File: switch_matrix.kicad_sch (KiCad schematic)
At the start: 8 parts, among them SW1 MX_SW_solder, SW2 MX_SW_solder, SW3 MX_SW_solder, SW4 MX_SW_solder

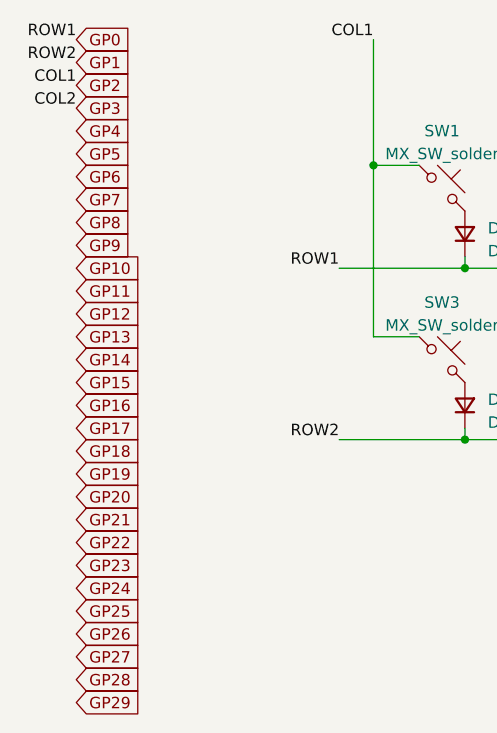
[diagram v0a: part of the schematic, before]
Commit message: update to kicad 8
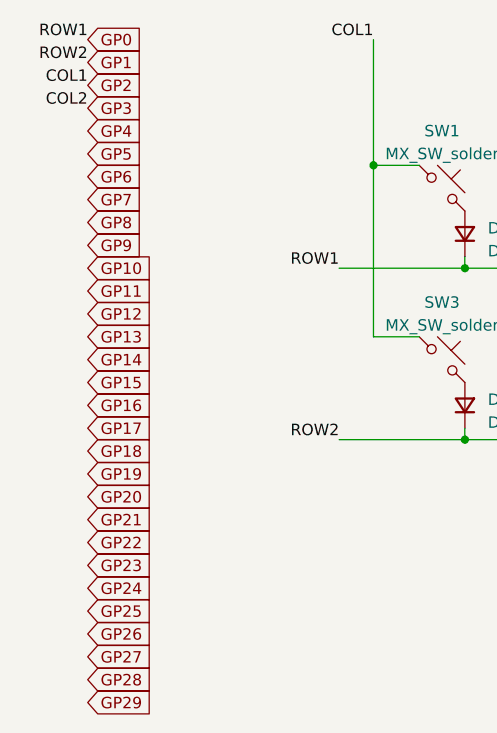
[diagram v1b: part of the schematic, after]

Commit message: keyboard switch comletion
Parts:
- removed D2, D4: D_Small, Diode_SMD:D_SOD-123, symbol Device:D_Small
- removed SW2, SW4: MX_SW_solder, marbastlib-mx:SW_MX_1u, symbol marbastlib-mx:MX_SW_solder
- added D203, D204, D205, D206, D207, D208, D209, D210, D211, D212, D213, D214, D215, D216, D217, D218, D219, D220, D221, D222, D223, D224, D225, D226, D227, D228, D229, D230, D231, D232, D233, D234, D235, D236, D237, D238, D239, D240, D241, D242, D243, D244, D245, D246, D247, D248, D249, D250, D251, D252, D253, D254, D255, D256, D257, D258, D259, D260, D261: D_Small, Diode_SMD:D_SOD-123, symbol Device:D_Small
- added SW203, SW204, SW205, SW206, SW207, SW208, SW209, SW210, SW211, SW212, SW213, SW214, SW215, SW216, SW217, SW218, SW219, SW220, SW221, SW222, SW223, SW224, SW225, SW226, SW227, SW228, SW229, SW230, SW231, SW232, SW233, SW234, SW235, SW236, SW237, SW238, SW239, SW240, SW241, SW242, SW243, SW244, SW245, SW246, SW247, SW248, SW249, SW250, SW251, SW252, SW253, SW254, SW255, SW256, SW257, SW258, SW259, SW260, SW261: MX_SW_solder, marbastlib-mx:SW_MX_1u, symbol marbastlib-mx:MX_SW_solder
- renumbered D1 to D201, D3 to D202, SW1 to SW201, SW3 to SW202
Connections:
- net GP0: now also SW201.1, SW202.1, SW203.1, SW204.1, SW205.1; no longer D201.1 (K)
- net GP1: now also SW206.1, SW207.1, SW208.1, SW209.1, SW210.1; no longer D202.1 (K)
- net GP10: now also SW246.1, SW247.1, SW248.1, SW249.1, SW250.1
- net GP11: now also SW251.1, SW252.1, SW253.1
- net GP12: now also SW255.1, SW256.1
- net GP13: now also SW257.1, SW258.1, SW259.1, SW260.1, SW261.1
- net GP14: now also D201.1 (K), D206.1 (K), D211.1 (K), D216.1 (K), D220.1 (K), D224.1 (K), D229.1 (K), D233.1 (K), D237.1 (K), D241.1 (K), D246.1 (K), D251.1 (K), D255.1 (K), D257.1 (K)
- net GP15: now also D202.1 (K), D207.1 (K), D212.1 (K), D217.1 (K), D221.1 (K), D225.1 (K), D230.1 (K), D234.1 (K), D238.1 (K), D242.1 (K), D247.1 (K), D252.1 (K), D256.1 (K), D258.1 (K)
- net GP16: now also D203.1 (K), D208.1 (K), D213.1 (K), D218.1 (K), D222.1 (K), D226.1 (K), D231.1 (K), D235.1 (K), D239.1 (K), D243.1 (K), D248.1 (K), D253.1 (K), D259.1 (K)
- net GP17: now also D204.1 (K), D209.1 (K), D214.1 (K), D219.1 (K), D223.1 (K), D227.1 (K), D232.1 (K), D236.1 (K), D240.1 (K), D244.1 (K), D249.1 (K), D260.1 (K)
- net GP18: now also D205.1 (K), D210.1 (K), D215.1 (K), D228.1 (K), D245.1 (K), D250.1 (K), D254.1 (K), D261.1 (K)
- net GP2: now also SW211.1, SW212.1, SW213.1, SW214.1, SW215.1; no longer SW201.1, SW202.1
- net GP3: now also SW216.1, SW217.1, SW218.1, SW219.1
- net GP4: now also SW220.1, SW221.1, SW222.1, SW223.1
- net GP5: now also SW224.1, SW225.1, SW226.1, SW227.1, SW228.1
- net GP6: now also SW229.1, SW230.1, SW231.1, SW232.1
- net GP7: now also SW233.1, SW234.1, SW235.1, SW236.1
- net GP8: now also SW237.1, SW238.1, SW239.1, SW240.1
- net GP9: now also SW241.1, SW242.1, SW243.1, SW244.1, SW245.1
- new net: D209.2 (A), SW209.2
- new net: D226.2 (A), SW226.2
- new net: D211.2 (A), SW211.2
- new net: D224.2 (A), SW224.2
- new net: D239.2 (A), SW239.2
- new net: D210.2 (A), SW210.2
- new net: D260.2 (A), SW260.2
- new net: D238.2 (A), SW238.2
- new net: D230.2 (A), SW230.2
- new net: D229.2 (A), SW229.2
- new net: D242.2 (A), SW242.2
- new net: D250.2 (A), SW250.2
- new net: D255.2 (A), SW255.2
- new net: D228.2 (A), SW228.2
- new net: D261.2 (A), SW261.2
- new net: D240.2 (A), SW240.2
- new net: D246.2 (A), SW246.2
- new net: D212.2 (A), SW212.2
- new net: D247.2 (A), SW247.2
- new net: D218.2 (A), SW218.2
- new net: D258.2 (A), SW258.2
- new net: D249.2 (A), SW249.2
- new net: D248.2 (A), SW248.2
- new net: D220.2 (A), SW220.2
- new net: D206.2 (A), SW206.2
- new net: D243.2 (A), SW243.2
- new net: D251.2 (A), SW251.2
- new net: D259.2 (A), SW259.2
- new net: D204.2 (A), SW204.2
- new net: D217.2 (A), SW217.2
- new net: D233.2 (A), SW233.2
- new net: D235.2 (A), SW235.2
- new net: D215.2 (A), SW215.2
- new net: D253.2 (A), SW253.2
- new net: D236.2 (A), SW236.2
- new net: D245.2 (A), SW245.2
- new net: D254.2 (A), SW254.2
- new net: D237.2 (A), SW237.2
- new net: D241.2 (A), SW241.2
- new net: D222.2 (A), SW222.2
- new net: D221.2 (A), SW221.2
- new net: D252.2 (A), SW252.2
- new net: D244.2 (A), SW244.2
- new net: D232.2 (A), SW232.2
- new net: D205.2 (A), SW205.2
- new net: D207.2 (A), SW207.2
- new net: D219.2 (A), SW219.2
- new net: D213.2 (A), SW213.2
- new net: D223.2 (A), SW223.2
- new net: D216.2 (A), SW216.2
- new net: D227.2 (A), SW227.2
- new net: D256.2 (A), SW256.2
- new net: D214.2 (A), SW214.2
- new net: D257.2 (A), SW257.2
- new net: D208.2 (A), SW208.2
- new net: D225.2 (A), SW225.2
- new net: D231.2 (A), SW231.2
- new net: D203.2 (A), SW203.2
- new net: D234.2 (A), SW234.2

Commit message: push de modification
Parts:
- A1: renamed from SW208; value MX_SW_solder -> LP Gateron; footprint marbastlib-mx:SW_MX_1u -> key_switch:SW_Gateron_LowProfile_THT
- B1: renamed from SW227; value MX_SW_solder -> LP Gateron; footprint marbastlib-mx:SW_MX_1u -> key_switch:SW_Gateron_LowProfile_THT
- C18: renamed from SW219; value MX_SW_solder -> LP Gateron; footprint marbastlib-mx:SW_MX_1u -> key_switch:SW_Gateron_LowProfile_THT
- D18: renamed from SW218; value MX_SW_solder -> LP Gateron; footprint marbastlib-mx:SW_MX_1u -> key_switch:SW_Gateron_LowProfile_THT
- E1: renamed from SW217; value MX_SW_solder -> LP Gateron; footprint marbastlib-mx:SW_MX_1u -> key_switch:SW_Gateron_LowProfile_THT
- F1: renamed from SW222; value MX_SW_solder -> LP Gateron; footprint marbastlib-mx:SW_MX_1u -> key_switch:SW_Gateron_LowProfile_THT
- G1: renamed from SW226; value MX_SW_solder -> LP Gateron; footprint marbastlib-mx:SW_MX_1u -> key_switch:SW_Gateron_LowProfile_THT
- H1: renamed from SW231; value MX_SW_solder -> LP Gateron; footprint marbastlib-mx:SW_MX_1u -> key_switch:SW_Gateron_LowProfile_THT
- I1: renamed from SW238; value MX_SW_solder -> LP Gateron; footprint marbastlib-mx:SW_MX_1u -> key_switch:SW_Gateron_LowProfile_THT
- J1: renamed from SW235; value MX_SW_solder -> LP Gateron; footprint marbastlib-mx:SW_MX_1u -> key_switch:SW_Gateron_LowProfile_THT
- K1: renamed from SW239; value MX_SW_solder -> LP Gateron; footprint marbastlib-mx:SW_MX_1u -> key_switch:SW_Gateron_LowProfile_THT
- KB"1: renamed from SW253; value MX_SW_solder -> LP Gateron; footprint marbastlib-mx:SW_MX_1u -> key_switch:SW_Gateron_LowProfile_THT
- KB+1: renamed from SW255; value MX_SW_solder -> LP Gateron; footprint marbastlib-mx:SW_MX_1u -> key_switch:SW_Gateron_LowProfile_THT
- KB-1: renamed from SW251; value MX_SW_solder -> LP Gateron; footprint marbastlib-mx:SW_MX_1u -> key_switch:SW_Gateron_LowProfile_THT
- KB1: renamed from SW206; value MX_SW_solder -> LP Gateron; footprint marbastlib-mx:SW_MX_1u -> key_switch:SW_Gateron_LowProfile_THT
- KB10: renamed from SW246; value MX_SW_solder -> LP Gateron; footprint marbastlib-mx:SW_MX_1u -> key_switch:SW_Gateron_LowProfile_THT
- KB2: renamed from SW211; value MX_SW_solder -> LP Gateron; footprint marbastlib-mx:SW_MX_1u -> key_switch:SW_Gateron_LowProfile_THT
- KB3: renamed from SW216; value MX_SW_solder -> LP Gateron; footprint marbastlib-mx:SW_MX_1u -> key_switch:SW_Gateron_LowProfile_THT
- KB4: renamed from SW220; value MX_SW_solder -> LP Gateron; footprint marbastlib-mx:SW_MX_1u -> key_switch:SW_Gateron_LowProfile_THT
- KB5: renamed from SW224; value MX_SW_solder -> LP Gateron; footprint marbastlib-mx:SW_MX_1u -> key_switch:SW_Gateron_LowProfile_THT
- KB6: renamed from SW229; value MX_SW_solder -> LP Gateron; footprint marbastlib-mx:SW_MX_1u -> key_switch:SW_Gateron_LowProfile_THT
- KB7: renamed from SW233; value MX_SW_solder -> LP Gateron; footprint marbastlib-mx:SW_MX_1u -> key_switch:SW_Gateron_LowProfile_THT
- KB8: renamed from SW237; value MX_SW_solder -> LP Gateron; footprint marbastlib-mx:SW_MX_1u -> key_switch:SW_Gateron_LowProfile_THT
- KB9: renamed from SW241; value MX_SW_solder -> LP Gateron; footprint marbastlib-mx:SW_MX_1u -> key_switch:SW_Gateron_LowProfile_THT
- KB:1: renamed from SW248; value MX_SW_solder -> LP Gateron; footprint marbastlib-mx:SW_MX_1u -> key_switch:SW_Gateron_LowProfile_THT
- KB<1: renamed from SW240; value MX_SW_solder -> LP Gateron; footprint marbastlib-mx:SW_MX_1u -> key_switch:SW_Gateron_LowProfile_THT
- KB>1: renamed from SW244; value MX_SW_solder -> LP Gateron; footprint marbastlib-mx:SW_MX_1u -> key_switch:SW_Gateron_LowProfile_THT
- KB>2: renamed from SW249; value MX_SW_solder -> LP Gateron; footprint marbastlib-mx:SW_MX_1u -> key_switch:SW_Gateron_LowProfile_THT
- KB\1: renamed from SW258; value MX_SW_solder -> LP Gateron; footprint marbastlib-mx:SW_MX_1u -> key_switch:SW_Gateron_LowProfile_THT
- KB_BS1: renamed from SW257; value MX_SW_solder -> LP Gateron; footprint marbastlib-mx:SW_MX_1u -> key_switch:SW_Gateron_LowProfile_THT
- KB_CL1: renamed from SW203; value MX_SW_solder -> LP Gateron; footprint marbastlib-mx:SW_MX_1u -> key_switch:SW_Gateron_LowProfile_THT
- KB_COM1: renamed from SW210; value MX_SW_solder -> LP Gateron; footprint marbastlib-mx:SW_MX_1u -> key_switch:SW_Gateron_LowProfile_THT
- KB_ESC1: renamed from SW201; value MX_SW_solder -> LP Gateron; footprint marbastlib-mx:SW_MX_1u -> key_switch:SW_Gateron_LowProfile_THT
- KB_FN1: renamed from SW250; value MX_SW_solder -> LP Gateron; footprint marbastlib-mx:SW_MX_1u -> key_switch:SW_Gateron_LowProfile_THT
- KB_L_ALT1: renamed from SW215; value MX_SW_solder -> LP Gateron; footprint marbastlib-mx:SW_MX_1u -> key_switch:SW_Gateron_LowProfile_THT
- KB_L_CTLR1: renamed from SW205; value MX_SW_solder -> LP Gateron; footprint marbastlib-mx:SW_MX_1u -> key_switch:SW_Gateron_LowProfile_THT
- KB_L_SHIFT1: renamed from SW204; value MX_SW_solder -> LP Gateron; footprint marbastlib-mx:SW_MX_1u -> key_switch:SW_Gateron_LowProfile_THT
- KB_MENU1: renamed from SW254; value MX_SW_solder -> LP Gateron; footprint marbastlib-mx:SW_MX_1u -> key_switch:SW_Gateron_LowProfile_THT
- KB_R_ALT1: renamed from SW245; value MX_SW_solder -> LP Gateron; footprint marbastlib-mx:SW_MX_1u -> key_switch:SW_Gateron_LowProfile_THT
- KB_R_CTRL1: renamed from SW261; value MX_SW_solder -> LP Gateron; footprint marbastlib-mx:SW_MX_1u -> key_switch:SW_Gateron_LowProfile_THT
- KB_R_SHIFT1: renamed from SW260; value MX_SW_solder -> LB Gateron; footprint marbastlib-mx:SW_MX_1u -> key_switch:SW_Gateron_LowProfile_THT
- KB_SPACE1: renamed from SW228; value MX_SW_solder -> LP Gateron; footprint marbastlib-mx:SW_MX_1u -> key_switch:SW_Gateron_LowProfile_THT
- KB_TAB1: renamed from SW202; value MX_SW_solder -> LP Gateron; footprint marbastlib-mx:SW_MX_1u -> key_switch:SW_Gateron_LowProfile_THT
- KB_enter1: renamed from SW259; value MX_SW_solder -> LP Gateron; footprint marbastlib-mx:SW_MX_1u -> key_switch:SW_Gateron_LowProfile_THT
- KB{1: renamed from SW252; value MX_SW_solder -> LP Gateron; footprint marbastlib-mx:SW_MX_1u -> key_switch:SW_Gateron_LowProfile_THT
- KB}1: renamed from SW256; value MX_SW_solder -> LP Gateron; footprint marbastlib-mx:SW_MX_1u -> key_switch:SW_Gateron_LowProfile_THT
- L1: renamed from SW243; value MX_SW_solder -> LP Gateron; footprint marbastlib-mx:SW_MX_1u -> key_switch:SW_Gateron_LowProfile_THT
- M1: renamed from SW236; value MX_SW_solder -> LP Gateron; footprint marbastlib-mx:SW_MX_1u -> key_switch:SW_Gateron_LowProfile_THT
- N1: renamed from SW232; value MX_SW_solder -> LP Gateron; footprint marbastlib-mx:SW_MX_1u -> key_switch:SW_Gateron_LowProfile_THT
- O1: renamed from SW242; value MX_SW_solder -> LP Gateron; footprint marbastlib-mx:SW_MX_1u -> key_switch:SW_Gateron_LowProfile_THT
- P1: renamed from SW247; value MX_SW_solder -> LP Gateron; footprint marbastlib-mx:SW_MX_1u -> key_switch:SW_Gateron_LowProfile_THT
- Q1: renamed from SW207; value MX_SW_solder -> LP Gateron; footprint marbastlib-mx:SW_MX_1u -> key_switch:SW_Gateron_LowProfile_THT
- R6: renamed from SW221; value MX_SW_solder -> LP Gateron; footprint marbastlib-mx:SW_MX_1u -> key_switch:SW_Gateron_LowProfile_THT
- S1: renamed from SW213; value MX_SW_solder -> LP Gateron; footprint marbastlib-mx:SW_MX_1u -> key_switch:SW_Gateron_LowProfile_THT
- T1: renamed from SW225; value MX_SW_solder -> LP Gateron; footprint marbastlib-mx:SW_MX_1u -> key_switch:SW_Gateron_LowProfile_THT
- U4: renamed from SW234; value MX_SW_solder -> LP Gateron; footprint marbastlib-mx:SW_MX_1u -> key_switch:SW_Gateron_LowProfile_THT
- V1: renamed from SW223; value MX_SW_solder -> LP Gateron; footprint marbastlib-mx:SW_MX_1u -> key_switch:SW_Gateron_LowProfile_THT
- W1: renamed from SW212; value MX_SW_solder -> LP Gateron; footprint marbastlib-mx:SW_MX_1u -> key_switch:SW_Gateron_LowProfile_THT
- X1: renamed from SW214; value MX_SW_solder -> LP Gateron; footprint marbastlib-mx:SW_MX_1u -> key_switch:SW_Gateron_LowProfile_THT
- Y2: renamed from SW230; value MX_SW_solder -> LP Gateron; footprint marbastlib-mx:SW_MX_1u -> key_switch:SW_Gateron_LowProfile_THT
- Z1: renamed from SW209; value MX_SW_solder -> LP Gateron; footprint marbastlib-mx:SW_MX_1u -> key_switch:SW_Gateron_LowProfile_THT
- renumbered D208 to D10, D209 to D11, D210 to D12, D211 to D13, D212 to D14, D213 to D15, D214 to D16, D215 to D17, D216 to D19, D217 to D20, D218 to D21, D219 to D22, D220 to D23, D221 to D24, D222 to D25, D223 to D26, D224 to D27, D225 to D28, D226 to D29, D201 to D3, D227 to D30, D228 to D31, D229 to D32, D230 to D33, D231 to D34, D232 to D35, D233 to D36, D234 to D37, D235 to D38, D236 to D39, D202 to D4, D237 to D40, D238 to D41, D239 to D42, D240 to D43, D241 to D44, D242 to D45, D243 to D46, D244 to D47, D245 to D48, D246 to D49, D203 to D5, D247 to D50, D248 to D51, D249 to D52, D250 to D53, D251 to D54, D252 to D55, D253 to D56, D254 to D57, D255 to D58, D256 to D59, D204 to D6, D257 to D60, D258 to D61, D259 to D62, D260 to D63, D261 to D64, D205 to D7, D206 to D8, D207 to D9
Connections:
- net GP11: now also KB_MENU1.1
- no-connect marks 0 -> 10
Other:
- note added: "All diodes here should be 1N4148WQ SOD-123 package, all should be on the front of the PCB if possible"
